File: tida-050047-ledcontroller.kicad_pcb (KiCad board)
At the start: 4 copper layers, 50 x 175 mm, 117 parts, among them Q1 AOD424, Q2 AOD424, U1 TPS25750DRJKR, U10 XT30PW-F, U15 SB1045L_C2844167, U16 BQ7790400PWR, U17 SMTSO3015CTJ, U18 SMTSO3015CTJ, U19 SMTSO3015CTJ, U2 CAT24C256WI-GT3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

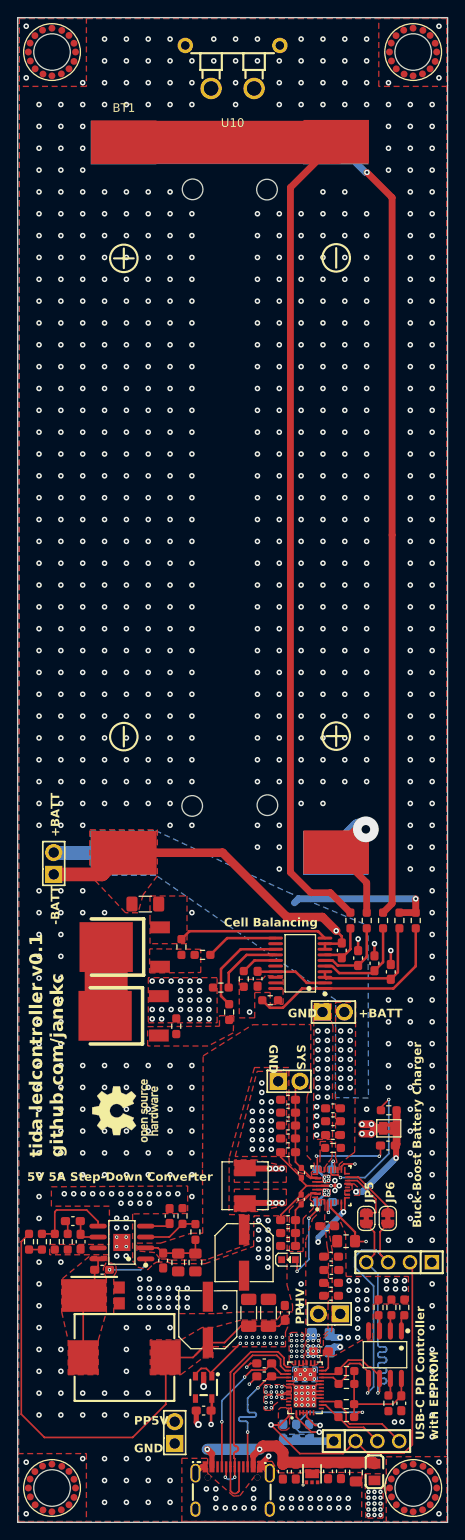
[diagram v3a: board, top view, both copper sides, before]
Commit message: replace battery protection with IC that actually balances the cells
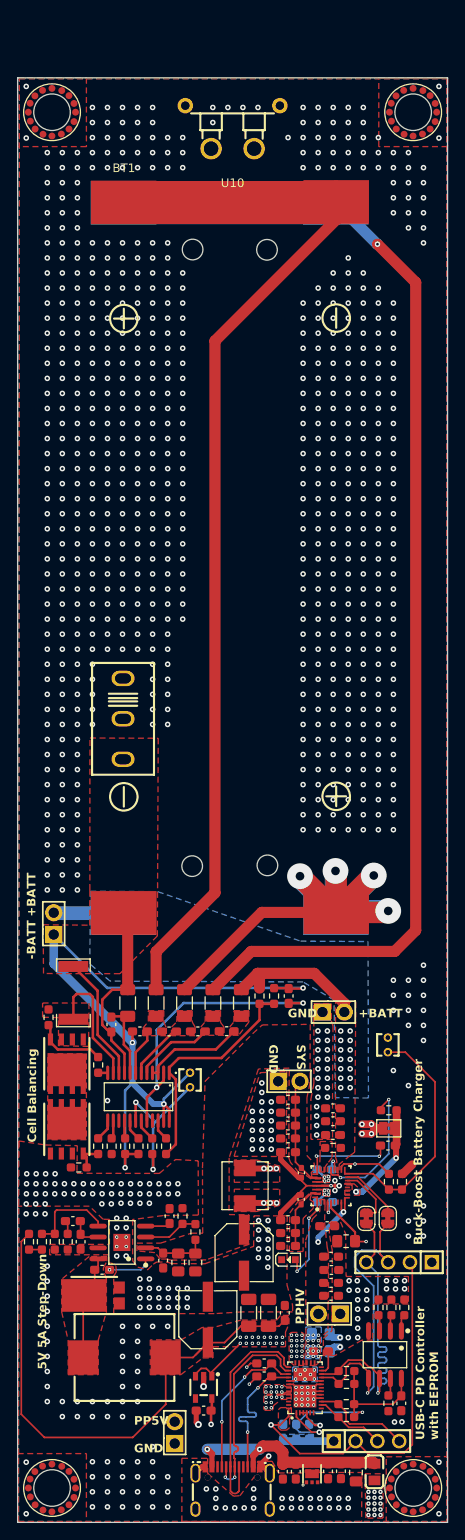
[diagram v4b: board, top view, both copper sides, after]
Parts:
- removed Q1, Q2: AOD424, easyeda2kicad:TO-252-3_L6.5-W6.1-P4.58-LS9.9-BR
- removed R29: 13m, Resistor_SMD:R_1206_3216Metric_Pad1.30x1.75mm_HandSolder
- removed R35: 10k, Resistor_SMD:R_0603_1608Metric_Pad0.98x0.95mm_HandSolder
- removed U16: BQ7790400PWR, easyeda2kicad:TSSOP-20_L6.5-W4.4-P0.65-LS6.4-BL
- added C62: 100nF, Capacitor_SMD:C_0603_1608Metric_Pad1.08x0.95mm_HandSolder, F.Cu at (131.2, 143.7)
- added Q3: IRFH5302TRPBF, easyeda2kicad:PQFN-8_L6.0-W5.0-P1.27-LS6.0-BL, F.Cu at (122.7, 155.0)
- added Q4: IRFH5302TRPBF, easyeda2kicad:PQFN-8_L6.0-W5.0-P1.27-LS6.0-BL, F.Cu at (122.7, 147.4)
- added R17: 30.31k, Resistor_SMD:R_0603_1608Metric_Pad0.98x0.95mm_HandSolder, F.Cu at (161.7, 161.1)
- added R18: 5.24k, Resistor_SMD:R_0603_1608Metric_Pad0.98x0.95mm_HandSolder, F.Cu at (160.2, 161.1)
- added R19: 103AT-4-050, easyeda2kicad:RES-TH_L2.5-W2.5-P1.70-D0.3, F.Cu at (137.1, 149.3)
- added R20: 103AT-4-050, easyeda2kicad:RES-TH_L2.5-W2.5-P1.70-D0.3, F.Cu at (160.1, 145.2)
- added R21: 10k, Resistor_SMD:R_0603_1608Metric_Pad0.98x0.95mm_HandSolder, F.Cu at (132.7, 157.0)
- added R22: 10k, Resistor_SMD:R_0603_1608Metric_Pad0.98x0.95mm_HandSolder, F.Cu at (134.3, 157.0)
- added R46: 75, Resistor_SMD:R_1206_3216Metric_Pad1.30x1.75mm_HandSolder, F.Cu at (129.8, 140.3)
- added R47: 100k, Resistor_SMD:R_0603_1608Metric_Pad0.98x0.95mm_HandSolder, F.Cu at (131.1, 157.0)
- added R48: 10k, Resistor_SMD:R_0603_1608Metric_Pad0.98x0.95mm_HandSolder, F.Cu at (129.5, 157.0)
- added SW1: SS-12M11G5, easyeda2kicad:SW-TH_XKB_SS-12M11XX, F.Cu at (129.3, 107.3)
- added U5: BQ7791502PWR, easyeda2kicad:TSSOP-24_L7.8-W4.4-P0.65-LS6.4-BL_1, F.Cu at (131.1, 151.2)
- added U6: HOYLR2512-3W-3MR-1%, easyeda2kicad:R2512, F.Cu at (123.5, 139.2)
- R25, R26, R27, R28: value 1K -> 75; footprint Resistor_SMD:R_0603_1608Metric_Pad0.98x0.95mm_HandSolder -> Resistor_SMD:R_1206_3216Metric_Pad1.30x1.75mm_HandSolder
- R30, R31: value 100k -> 1M
- R32: value 1k -> 4.5k
- R36: value 100R -> 1k
- moved C51 28.2 mm to (127.9, 142.8)
- moved R28 24.5 mm to (133.1, 140.3)
- moved C50 23.6 mm to (134.6, 143.7), turned to 180 degrees
- moved R27 23.3 mm to (136.4, 140.3)
- moved R34 22.4 mm to (127.9, 157.0), turned to -90 degrees
- moved C49 22.0 mm to (138.0, 143.7), turned to 180 degrees
- moved R26 22.0 mm to (139.7, 140.3)
- moved R33 21.8 mm to (126.4, 157.0), turned to -90 degrees
- moved R25 20.7 mm to (143.0, 140.3)
- moved C19 20.3 mm to (141.3, 143.6), turned to 180 degrees
- moved R36 20.2 mm to (145.1, 139.5)
- moved R31 20.0 mm to (124.1, 159.5), turned to 180 degrees
- moved R32 17.6 mm to (126.4, 147.6), turned to 90 degrees
- moved R30 17.5 mm to (120.6, 142.0)
- moved BT1 7.00 mm to (129.3, 88.6)
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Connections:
- C19 pad 2: -BATT -> Net-(U5-VC3)
- C49 pad 1: Net-(U16-VC3) -> Net-(U5-VC3)
- C49 pad 2: -BATT -> Net-(U5-VC2)
- C50 pad 1: Net-(U16-VC2) -> Net-(U5-VC2)
- C50 pad 2: -BATT -> Net-(U5-VC1)
- C51 pad 1: Net-(U16-VC1) -> -BATT
- C51 pad 2: -BATT -> Net-(U5-VCO)
- R26 pad 2: Net-(U16-VC3) -> Net-(U5-VC3)
- R27 pad 2: Net-(U16-VC2) -> Net-(U5-VC2)
- R28 pad 2: Net-(U16-VC1) -> Net-(U5-VC1)
- R30 pad 1: Net-(Q1-G) -> Net-(Q4-G)
- R31 pad 1: Net-(Q2-G) -> Net-(Q3-G)
- R32 pad 1: Net-(Q1-G) -> Net-(U5-DSG)
- R32 pad 2: Net-(U16-DSG) -> Net-(Q4-G)
- R33 pad 1: Net-(Q2-G) -> Net-(U5-CHG)
- R33 pad 2: Net-(U16-CHG) -> Net-(Q3-G)
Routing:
- net PP5V: track 232.1 -> 83.8 mm
- net -BATT: track 69.0 -> 122.6 mm, vias 5 -> 4
- net Net-(BT2-Pad2): track 17.7 -> 67.8 mm, vias 1 -> 4
- net TS: track 0.00 -> 28.4 mm
- net Net-(U5-AVDD): track 8.39 -> 33.8 mm, vias 0 -> 2
- net Net-(BT3-Pad2): track 117.5 -> 139.6 mm
- net Net-(U5-TS): track 0.00 -> 19.1 mm, vias 0 -> 2
- net Net-(U16-CHG): track 11.8 -> 0.00 mm
- net Net-(U16-VC3): track 11.6 -> 0.00 mm
- net Net-(U5-VC3): track 0.00 -> 9.23 mm
- net Net-(U5-VCO): track 0.00 -> 8.99 mm
- net Net-(U16-VC2): track 8.84 -> 0.00 mm
- net Net-(U16-DSG): track 8.40 -> 0.00 mm
- net Net-(Q4-G): track 0.00 -> 8.34 mm
- net Net-(Q1-D): track 8.05 -> 0.00 mm
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- added copper zone on F.Cu, net Net-(Q3-D-Pad5)
- added copper zone on F.Cu, net Net-(U5-VC1)
- added copper zone on F.Cu, net Net-(U5-VC2)
- added copper zone on F.Cu, net Net-(U5-VC3)
- added copper zone on F.Cu, net Net-(U5-VC4)
- added copper zone on B.Cu, net PPHV
- removed copper zone on F.Cu, net Net-(Q1-G)
- removed copper zone on F.Cu, net Net-(Q2-G)
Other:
- board size 50 x 175 mm -> 50 x 168 mm
- board text added: "5V 5A Step-Down"
- board text added: "I2C1_SCL I2C1_SDA 3V3 GND"
- board text removed: "5V 5A Step-Down Converter"

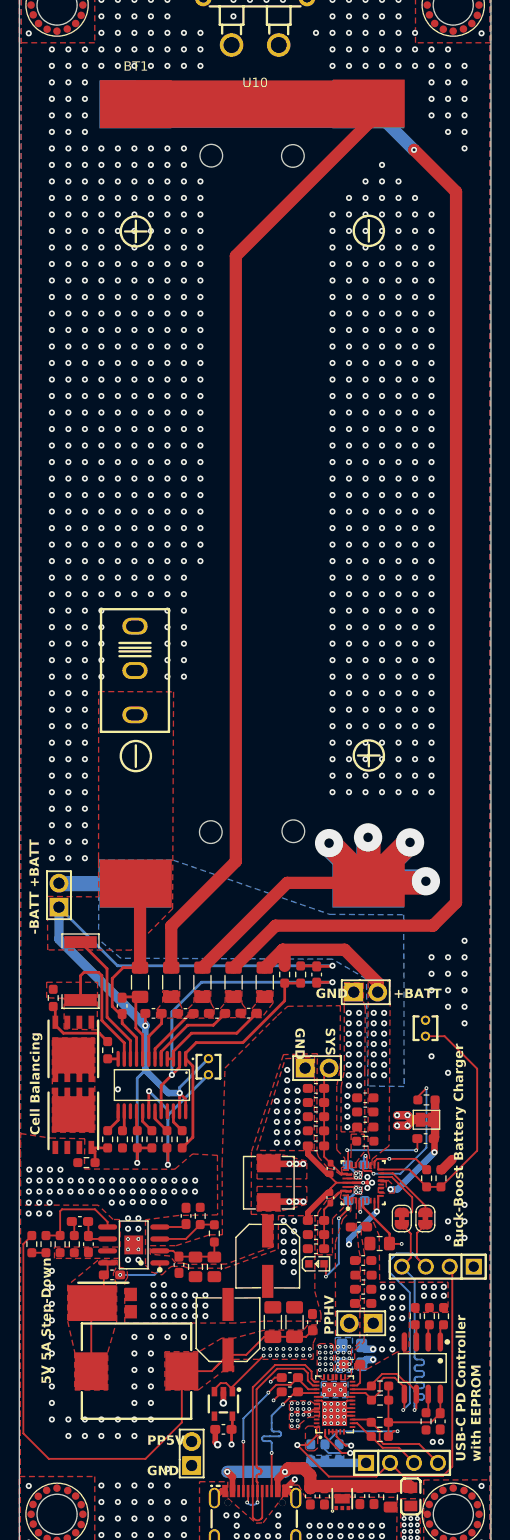
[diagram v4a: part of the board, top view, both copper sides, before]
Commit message: enlarge silkscreen font
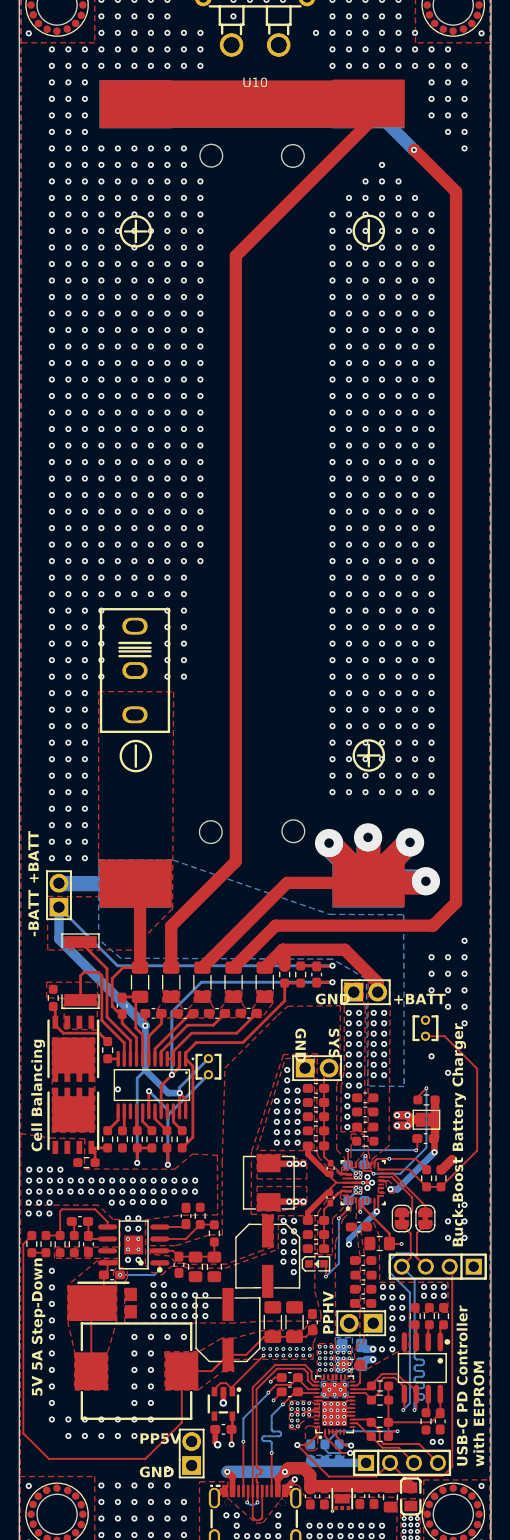
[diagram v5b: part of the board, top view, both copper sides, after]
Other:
- board text added: "GND 3V3 I2C1_SDA I2C1_SCL"
- board text added: "TIDA-PowerPack v0.1 github.com/janekc"
- board text removed: "tida-ledcontroller v0.1 github.com/janekc"
